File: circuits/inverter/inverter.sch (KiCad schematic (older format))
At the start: 0 parts

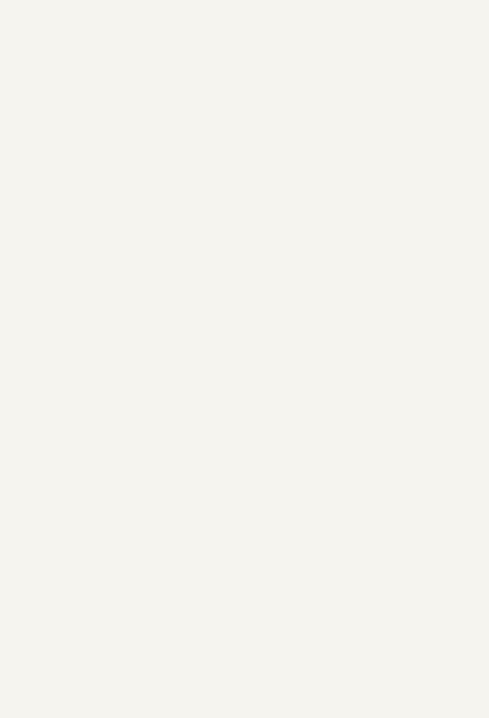
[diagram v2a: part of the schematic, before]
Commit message: bulk-updates libraries and schematics
schematic is updated to Kicad 5.1.14
updates various sheets with new circuits
adds various component libraries
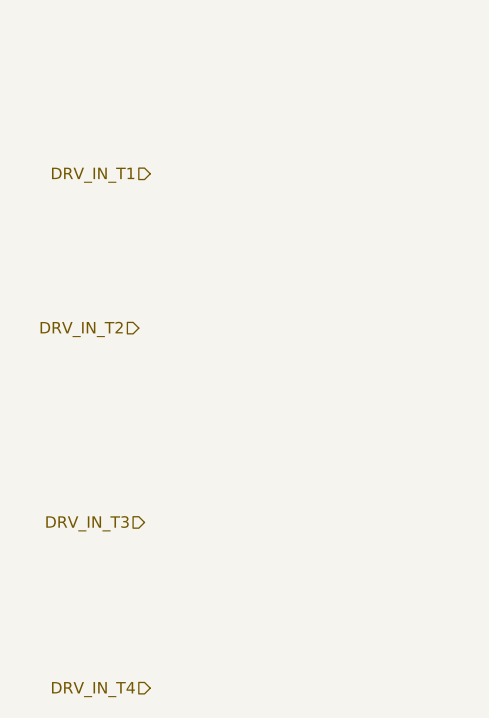
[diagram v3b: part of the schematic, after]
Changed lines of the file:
@@
-EESchema Schematic File Version 2
-LIBS:lm317
-LIBS:kv30f
-LIBS:OSSI_standard_components
-LIBS:connectors
-LIBS:lm4030
-LIBS:acs722
+EESchema Schematic File Version 4
 LIBS:OSSI_MK_I-cache
-EELAYER 25 0
+EELAYER 30 0
 EELAYER END
 $Descr A4 11693 8268
@@
 Text HLabel 10600 1400 2    60   Output ~ 0
 AC_Vtg_N
+Text HLabel 1150 2075 0    50   Input ~ 0
+DRV_IN_T1
+Text HLabel 1100 2750 0    50   Input ~ 0
+DRV_IN_T2
+Text HLabel 1125 3600 0    50   Input ~ 0
+DRV_IN_T3
+Text HLabel 1150 4325 0    50   Input ~ 0
+DRV_IN_T4
 $EndSCHEMATC

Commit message: minor updates and cleaup
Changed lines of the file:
@@
 EESchema Schematic File Version 4
-LIBS:OSSI_MK_I-cache
 EELAYER 30 0
 EELAYER END
 $Descr A4 11693 8268
 encoding utf-8
-Sheet 4 11
+Sheet 12 12
 Title ""
 Date ""
@@
 Text HLabel 10600 1400 2    60   Output ~ 0
 AC_Vtg_N
-Text HLabel 1150 2075 0    50   Input ~ 0
+Text HLabel 1125 1400 0    50   Input ~ 0
 DRV_IN_T1
 Text HLabel 1100 2750 0    50   Input ~ 0
@@
 Text HLabel 1150 4325 0    50   Input ~ 0
 DRV_IN_T4
+Text HLabel 1150 1000 0    50   Input ~ 0
+HSS1_+15V
+Text HLabel 1075 1775 0    50   Input ~ 0
+HSS1_GND
+Text HLabel 1150 3150 0    50   Input ~ 0
+HSS2_+15V
+Text HLabel 1125 3850 0    50   Input ~ 0
+HSS2_GND
 $EndSCHEMATC
